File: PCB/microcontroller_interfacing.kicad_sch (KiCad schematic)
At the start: 24 parts, among them U6 CH340C

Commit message: Update MC Interfacing schematic
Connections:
- net GPIO 1 is gone; now on net GPIO 0: J?.11 (Pin_11), J?.11 (Pin_11)
- net A0: now also J?.10 (Pin_10), J?.10 (Pin_10)
- net GPIO 0: no longer J?.10 (Pin_10), J?.10 (Pin_10)
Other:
- company: (none) -> University of Cape Town
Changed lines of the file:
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@@
     (date "2023-03-12")
     (rev "2")
+    (company "University of Cape Town")
     (comment 1 "Group 3")
-    (comment 2 "Authors: Adrian McIntosh, Simon Carthew, Michael Awe")
+    (comment 2 "Author: Michael Awe")
   )
   (junction (at 48.26 54.61) (diameter 0) (color 0 0 0 0)
@@
     (stroke (width 0) (type default))
   )
+  (wire (pts (xy 191.77 109.22) (xy 194.31 109.22))
+    (stroke (width 0) (type default))
+  )
   (wire (pts (xy 191.135 62.23) (xy 212.09 62.23))
     (stroke (width 0) (type default))
@@
     )
   )
-  (global_label "3V3" (shape input) (at 193.04 95.25 0) (fields_autoplaced)
-    (effects (font (size 1.27 1.27)) (justify left))
-    (property "Intersheetrefs" "${INTERSHEET_REFS}" (at 199.4534 95.25 0)
-      (effects (font (size 1.27 1.27)) (justify left) hide)
-    )
-  )
   (global_label "USB D-" (shape input) (at 151.13 43.18 0) (fields_autoplaced)
     (effects (font (size 1.27 1.27)) (justify left))
@@
     )
   )
-  (global_label "3V3" (shape input) (at 252.73 36.83 180) (fields_autoplaced)
-    (effects (font (size 1.27 1.27)) (justify right))
-    (property "Intersheetrefs" "${INTERSHEET_REFS}" (at 246.3166 36.83 0)
-      (effects (font (size 1.27 1.27)) (justify right) hide)
-    )
-  )
   (global_label "EEPROMSDA" (shape input) (at 191.77 90.17 0) (fields_autoplaced)
     (effects (font (size 1.27 1.27)) (justify left))
@@
     (effects (font (size 1.27 1.27)) (justify left))
     (property "Intersheetrefs" "${INTERSHEET_REFS}" (at 258.5991 80.01 0)
-      (effects (font (size 1.27 1.27)) (justify left) hide)
-    )
-  )
-  (global_label "3V3" (shape input) (at 191.77 57.15 0) (fields_autoplaced)
-    (effects (font (size 1.27 1.27)) (justify left))
-    (property "Intersheetrefs" "${INTERSHEET_REFS}" (at 198.1834 57.15 0)
       (effects (font (size 1.27 1.27)) (justify left) hide)
     )
@@
     )
   )
-  (global_label "3V3" (shape input) (at 209.55 128.27 90) (fields_autoplaced)
-    (effects (font (size 1.27 1.27)) (justify left))
-    (property "Intersheetrefs" "${INTERSHEET_REFS}" (at 209.55 121.8566 90)
-      (effects (font (size 1.27 1.27)) (justify left) hide)
-    )
-  )
   (global_label "USART_RX" (shape input) (at 67.31 96.52 0) (fields_autoplaced)
     (effects (font (size 1.27 1.27)) (justify left))
@@
     )
   )
-  (global_label "3V3" (shape input) (at 250.19 128.27 90) (fields_autoplaced)
-    (effects (font (size 1.27 1.27)) (justify left))
-    (property "Intersheetrefs" "${INTERSHEET_REFS}" (at 250.19 121.8566 90)
-      (effects (font (size 1.27 1.27)) (justify left) hide)
-    )
-  )
   (global_label "USART_TX" (shape input) (at 246.38 82.55 0) (fields_autoplaced)
     (effects (font (size 1.27 1.27)) (justify left))
     (property "Intersheetrefs" "${INTERSHEET_REFS}" (at 258.2967 82.55 0)
-      (effects (font (size 1.27 1.27)) (justify left) hide)
-    )
-  )
-  (global_label "3V3" (shape input) (at 129.54 83.82 90) (fields_autoplaced)
-    (effects (font (size 1.27 1.27)) (justify left))
-    (property "Intersheetrefs" "${INTERSHEET_REFS}" (at 129.54 77.4066 90)
       (effects (font (size 1.27 1.27)) (justify left) hide)
     )
@@
     (effects (font (size 1.27 1.27)) (justify left))
   )
+  (hierarchical_label "3V3" (shape input) (at 193.04 57.15 0) (fields_autoplaced)
+    (effects (font (size 1.27 1.27)) (justify left))
+  )
   (hierarchical_label "3V3" (shape input) (at 48.26 30.48 90) (fields_autoplaced)
     (effects (font (size 1.27 1.27)) (justify left))
   )
+  (hierarchical_label "3V3" (shape input) (at 247.65 36.83 0) (fields_autoplaced)
+    (effects (font (size 1.27 1.27)) (justify left))
+  )
   (hierarchical_label "USB 5V" (shape input) (at 62.23 104.14 0) (fields_autoplaced)
+    (effects (font (size 1.27 1.27)) (justify left))
+  )
+  (hierarchical_label "3V3" (shape input) (at 129.54 83.82 90) (fields_autoplaced)
+    (effects (font (size 1.27 1.27)) (justify left))
+  )
+  (hierarchical_label "GND" (shape bidirectional) (at 194.31 109.22 0) (fields_autoplaced)
     (effects (font (size 1.27 1.27)) (justify left))
   )
@@
     (effects (font (size 1.27 1.27)) (justify right))
   )
+  (hierarchical_label "3V3" (shape input) (at 193.04 95.25 0) (fields_autoplaced)
+    (effects (font (size 1.27 1.27)) (justify left))
+  )
+  (hierarchical_label "3V3" (shape input) (at 209.55 128.27 90) (fields_autoplaced)
+    (effects (font (size 1.27 1.27)) (justify left))
+  )
+  (hierarchical_label "3V3" (shape input) (at 250.19 128.27 90) (fields_autoplaced)
+    (effects (font (size 1.27 1.27)) (justify left))
+  )
   (hierarchical_label "DigitalSensorSCL" (shape input) (at 50.8 105.41 180) (fields_autoplaced)
     (effects (font (size 1.27 1.27)) (justify right))
@@
     (effects (font (size 1.27 1.27)) (justify left))
   )
-  (hierarchical_label "GPIO 0" (shape input) (at 191.77 59.69 0) (fields_autoplaced)
-    (effects (font (size 1.27 1.27)) (justify left))
-  )
-  (hierarchical_label "GPIO 1" (shape input) (at 191.77 62.23 0) (fields_autoplaced)
+  (hierarchical_label "A0" (shape input) (at 193.04 59.69 0) (fields_autoplaced)
+    (effects (font (size 1.27 1.27)) (justify left))
+  )
+  (hierarchical_label "GPIO 0" (shape input) (at 193.04 62.23 0) (fields_autoplaced)
     (effects (font (size 1.27 1.27)) (justify left))
   )
@@
         )
       )
+    )
+  )
+  (symbol (lib_id "power:GND") (at 191.77 109.22 270) (unit 1)
+    (in_bom yes) (on_board yes) (dnp no) (fields_autoplaced)
+    (property "Reference" "#PWR?" (at 185.42 109.22 0)
+      (effects (font (size 1.27 1.27)) hide)
+    )
+    (property "Value" "GND" (at 187.96 109.855 90)
+      (effects (font (size 1.27 1.27)) (justify right))
+    )
+    (property "Footprint" "" (at 191.77 109.22 0)
+      (effects (font (size 1.27 1.27)) hide)
+    )
+    (property "Datasheet" "" (at 191.77 109.22 0)
+      (effects (font (size 1.27 1.27)) hide)
+    )
+    (pin "1")
+    (instances
+      (project "Main"
+        (path "/1e9f3d34-a4c0-4684-8b0d-9d61663dabf9/dc5135c5-d6ed-4046-bf12-773bd1e5ac0e"
+          (reference "#PWR?") (unit 1)
+        )
+      )
+      (project "HAT"
+        (path "/40f36b19-a08c-43e7-88a6-ec8387939712/b7b1774d-5583-4628-a0c2-f9ec68f1422c"
+          (reference "#PWR035") (unit 1)
+        )
+      )
+      (project "EEE3088F"
+        (path "/55241c4b-74de-4f3f-ae14-f523593e7e6b"
+          (reference "#PWR?") (unit 1)
+        )
+      )

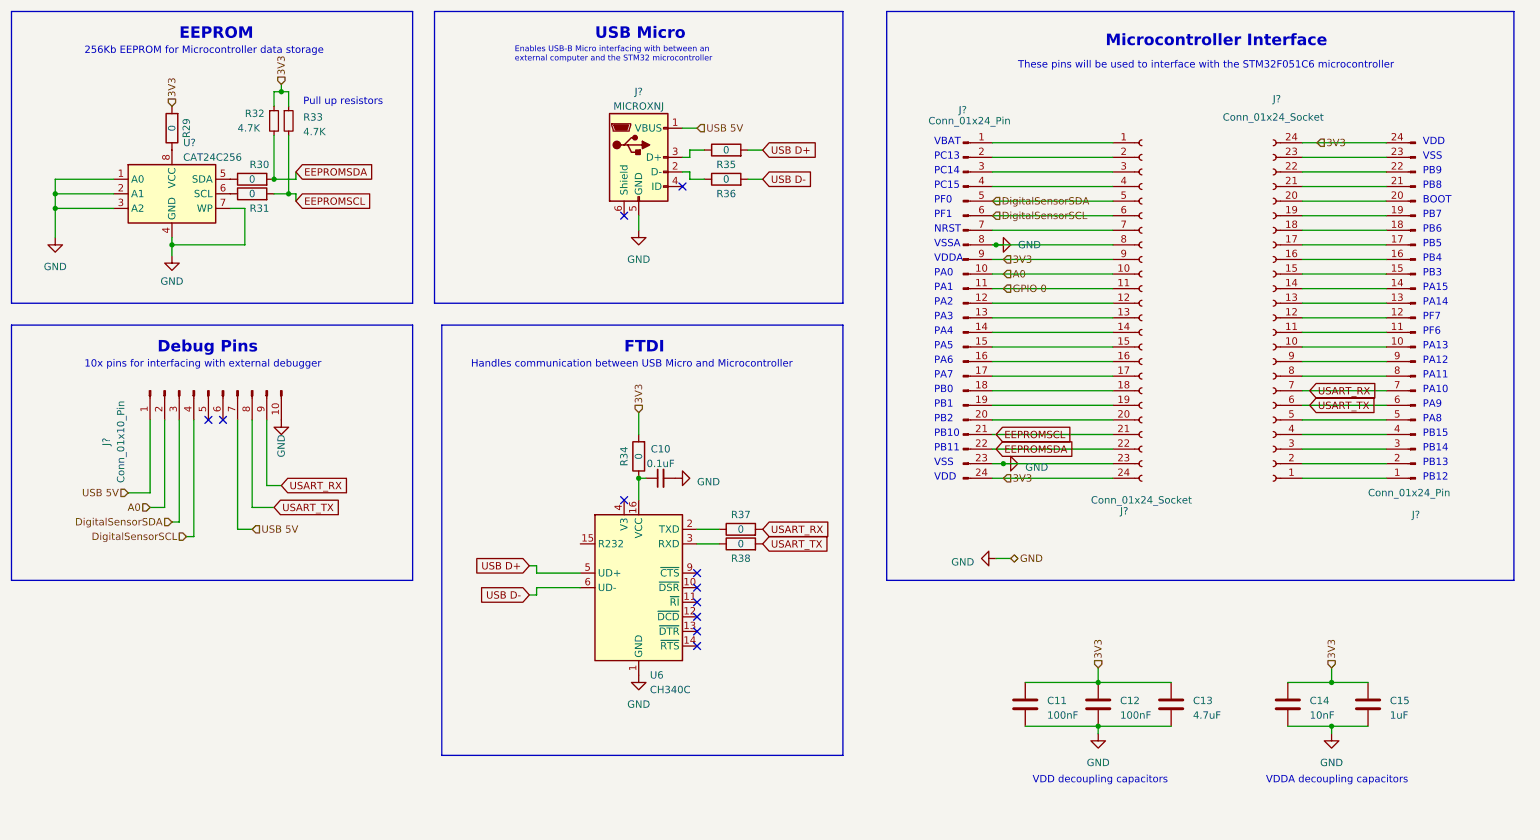
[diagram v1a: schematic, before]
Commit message: Add GND jumper pin to STM-32
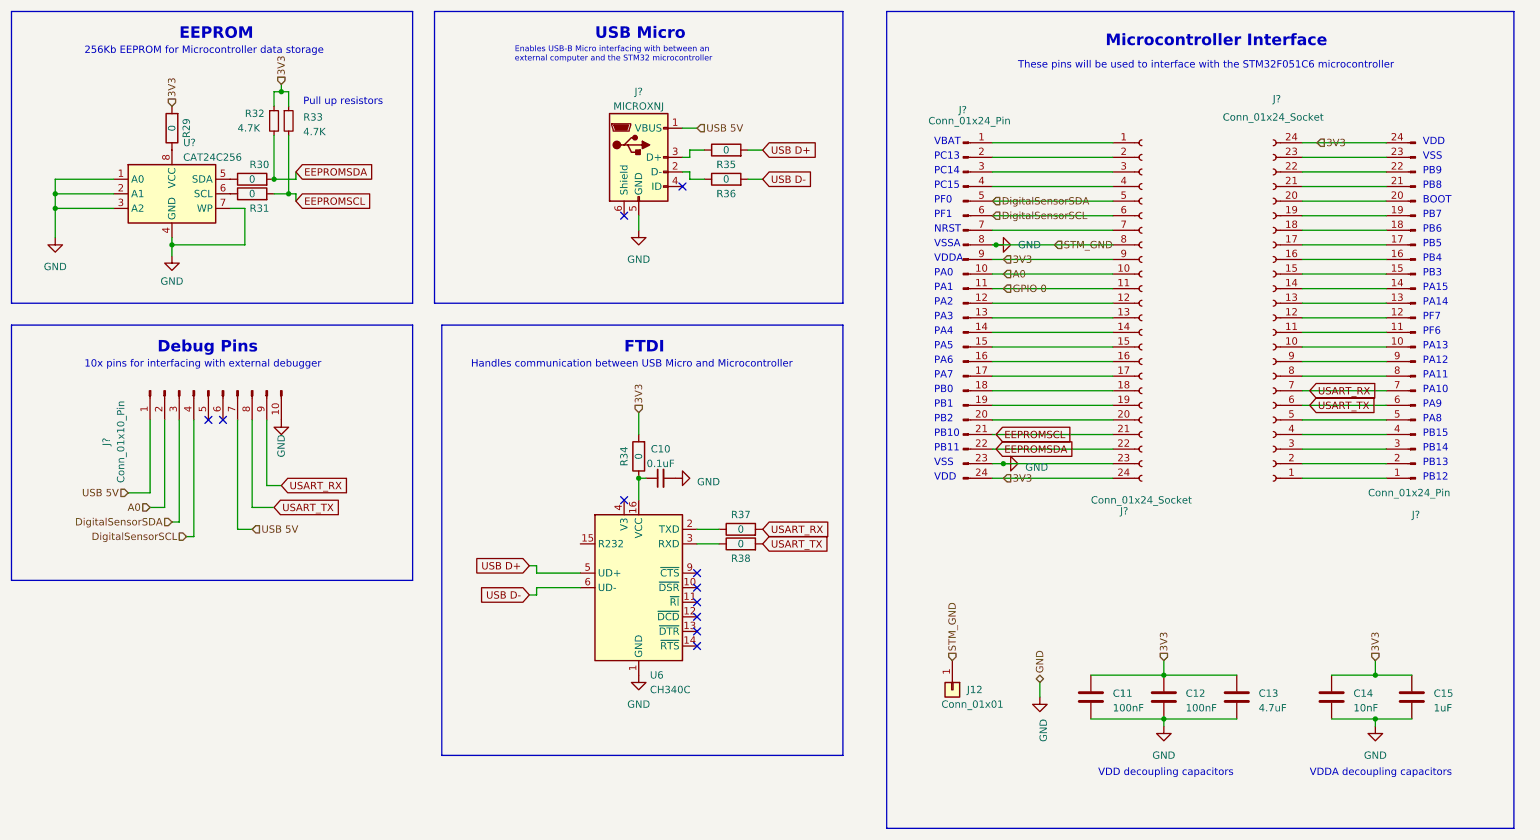
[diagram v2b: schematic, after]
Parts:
- added J12: Conn_01x01, symbol Connector_Generic:Conn_01x01
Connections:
- net GND: now also J12.1 (Pin_1)
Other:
- moved on the sheet: C11, C12, C13, C14, C15
